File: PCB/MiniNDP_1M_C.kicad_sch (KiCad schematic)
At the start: 12 parts, among them J1 Conn_02x20_Odd_Even, U1 HC238, U2 HC4040, U3 HC573, U4 AS6C2008A_DIP32_SOP32

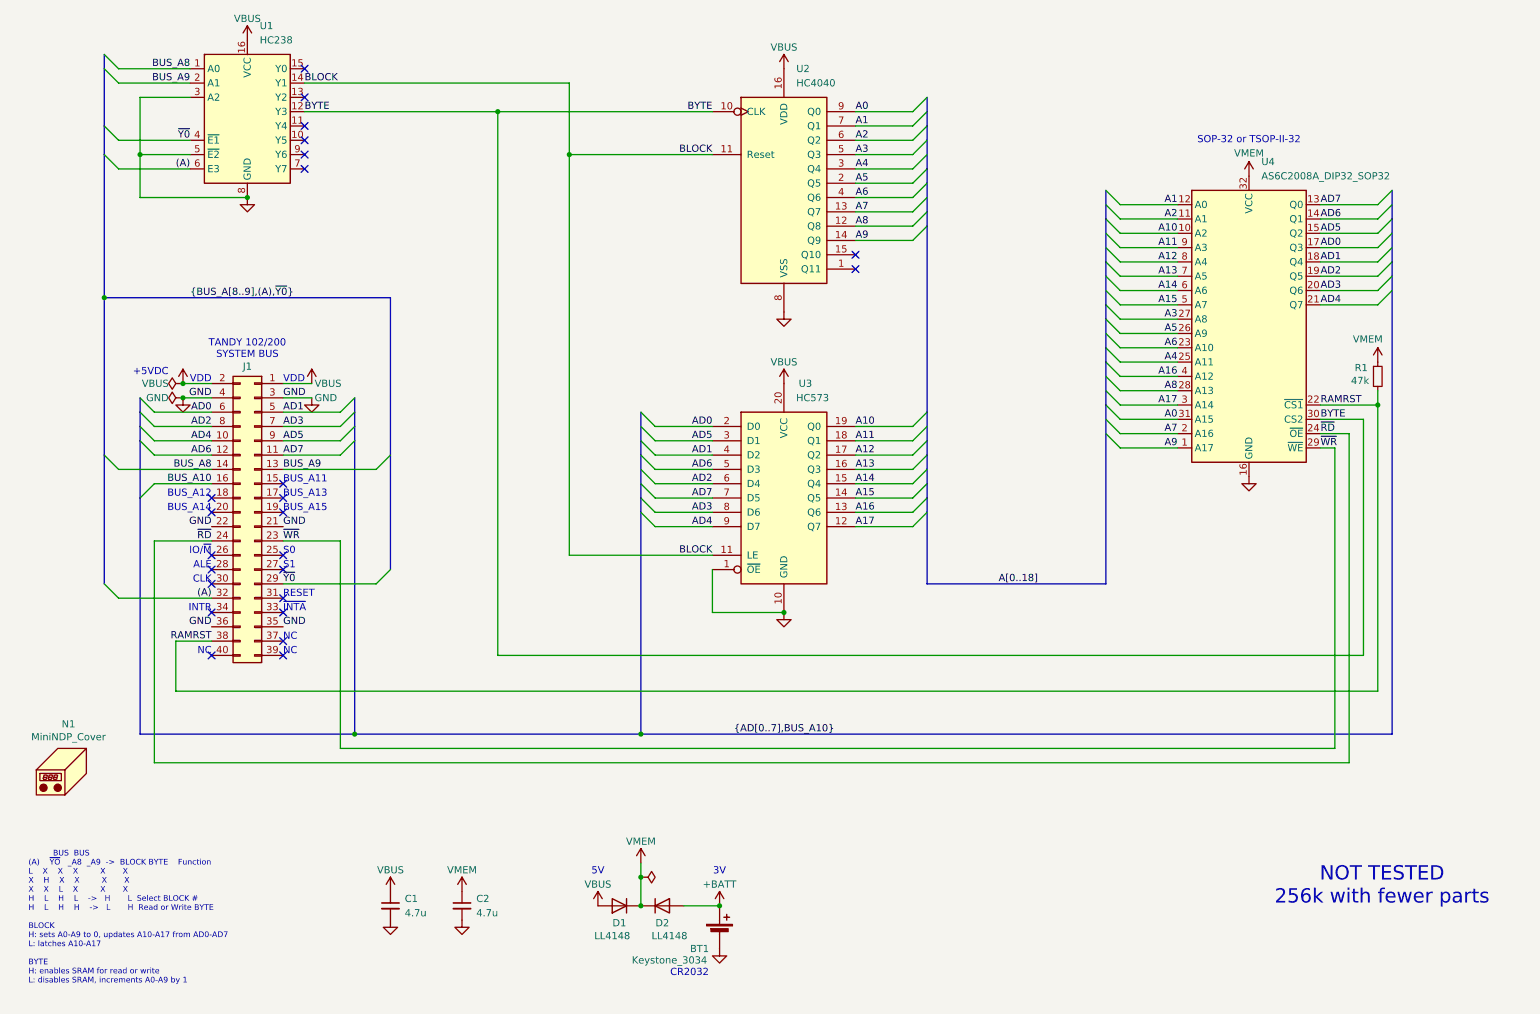
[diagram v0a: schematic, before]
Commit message: 1M_C 1 meg based on 4040
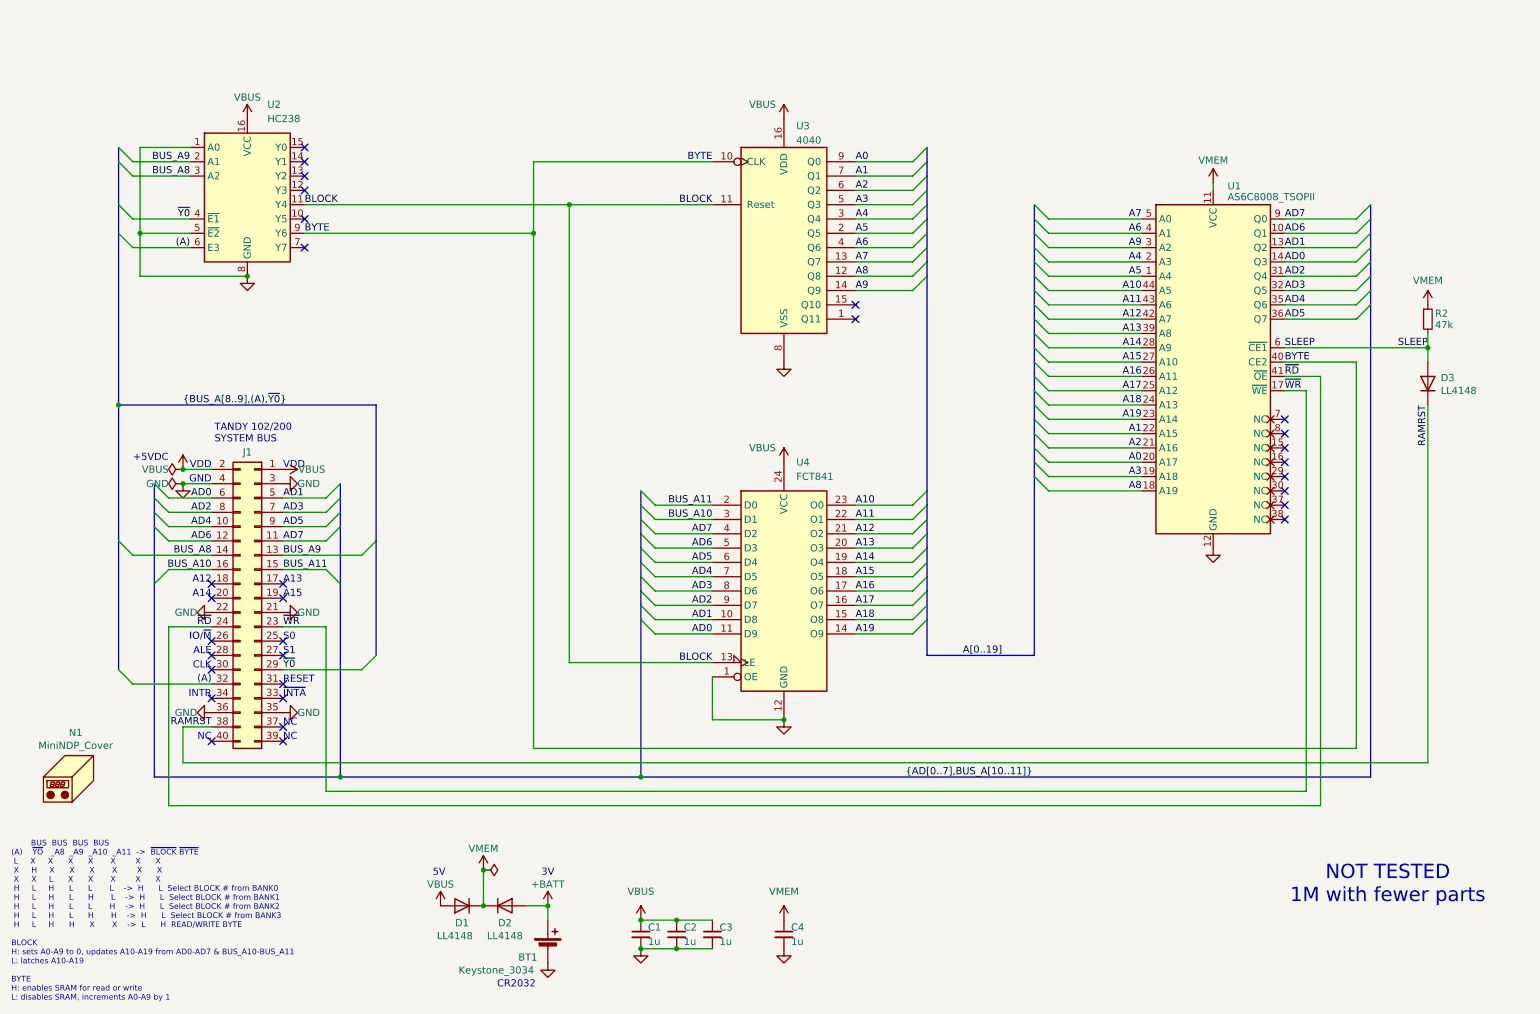
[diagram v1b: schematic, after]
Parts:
- removed R1: 47k, 000_LOCAL:R_1206, symbol 000_LOCAL:R
- removed U1: HC238, 000_LOCAL:SOIC-16_3.9x9.9mm_P1.27mm, symbol 000_LOCAL:74HC238
- removed U2: HC4040, 000_LOCAL:SOIC-16_3.9x9.9mm_P1.27mm, symbol 000_LOCAL:4040
- removed U3: HC573, 000_LOCAL:SOIC-20W_7.5x12.8mm_P1.27mm, symbol 000_LOCAL:74x573
- removed U4: AS6C2008A_DIP32_SOP32, 000_LOCAL:TSOP-II-SOP-32_dual, symbol 000_LOCAL:AS6C2008A_DIP32_SOP32
- added C3, C4: 1u, 000_LOCAL:C_0805, symbol 000_LOCAL:C
- added D3: LL4148, 000_LOCAL:D_MiniMELF, symbol 000_LOCAL:LL4148
- added R2: 47k, 000_LOCAL:R_0805, symbol 000_LOCAL:R
- added U1: AS6C8008_TSOPII, 000_LOCAL:TSOP-II-44, symbol 000_LOCAL:AS6C8008_TSOPII
- added U2: HC238, 000_LOCAL:SOIC-16_3.9x9.9mm_P1.27mm, symbol 000_LOCAL:HC238
- added U3: 4040, 000_LOCAL:SOIC-16_3.9x9.9mm_P1.27mm, symbol 000_LOCAL:4040
- added U4: FCT841, 000_LOCAL:SOIC-24, symbol 000_LOCAL:FCT841
- C1, C2: value 4.7u -> 1u; footprint 000_LOCAL:C_1206 -> 000_LOCAL:C_0805; MPN CL31B475KAHNNNE -> CL21B105KAFNNNE
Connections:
- net (A): now also U2.6 (E3)
- net A0: now also U1.20 (A17), U3.9 (Q0)
- net A1: now also U1.22 (A15), U3.7 (Q1)
- net A10: now also U1.44 (A5), U4.23 (O0)
- net A11: now also U1.43 (A6), U4.22 (O1)
- net A12: now also U1.42 (A7), U4.21 (O2)
- net A13: now also U1.39 (A8), U4.20 (O3)
- net A14: now also U1.28 (A9), U4.19 (O4)
- net A15: now also U1.27 (A10), U4.18 (O5)
- net A16: now also U1.26 (A11), U4.17 (O6)
- net A17: now also U1.25 (A12), U4.16 (O7)
- net A2: now also U1.21 (A16), U3.6 (Q2)
- net A3: now also U1.19 (A18), U3.5 (Q3)
- net A4: now also U1.2 (A3), U3.3 (Q4)
- net A5: now also U1.1 (A4), U3.2 (Q5)
- net A6: now also U1.4 (A1), U3.4 (Q6)
- net A7: now also U1.5 (A0), U3.13 (Q7)
- net A8: now also U1.18 (A19), U3.12 (Q8)
- net A9: now also U1.3 (A2), U3.14 (Q9)
- net AD0: now also U1.14 (Q3), U4.11 (D9)
- net AD1: now also U1.13 (Q2), U4.10 (D8)
- net AD2: now also U1.31 (Q4), U4.9 (D7)
- net AD3: now also U1.32 (Q5), U4.8 (D6)
- net AD4: now also U1.35 (Q6), U4.7 (D5)
- net AD5: now also U1.36 (Q7), U4.6 (D4)
- net AD6: now also U1.10 (Q1), U4.5 (D3)
- net AD7: now also U1.9 (Q0), U4.4 (D2)
- net BLOCK: now also U2.11 (Y4), U3.11 (Reset), U4.13 (LE)
- net BUS_A10: now also U4.3 (D1)
- net BUS_A8: now also U2.3 (A2)
- net BUS_A9: now also U2.2 (A1)
- net BYTE: now also U1.40 (CE2), U2.9 (Y6), U3.10 (CLK)
- net GND: now also C3.2, C4.2, U1.12 (GND), U1.34 (GND), U2.1 (A0), U2.5 (~{E2}), U2.8 (GND), U3.8 (VSS), U4.1 (OE), U4.12 (GND)
- net RAMRST: now also D3.1 (K)
- net VBUS: now also C2.1, C3.1, U2.16 (VCC), U3.16 (VDD), U4.24 (VCC)
- net VMEM: now also C4.1, R2.1, U1.11 (VCC), U1.33 (VCC); no longer C2.1
- net ~{RD}: now also U1.41 (~{OE})
- net ~{WR}: now also U1.17 (~{WE})
- net ~{Y0}: now also U2.4 (~{E1})
- net BUS_A11: now reaches J1.15 (Pin_15)
- net BUS_A11: now also U4.2 (D0)
- new net A18: U1.24 (A13), U4.15 (O8)
- new net A19: U1.23 (A14), U4.14 (O9)
- new net SLEEP: D3.2 (A), R2.2, U1.6 (~{CE1})
- no-connect marks 24 -> 31
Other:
- note added: "A12"
- note added: "A13"
- note added: "A14"
- note added: "A15"
- note added: "BUS BUS BUS BUS (A) ~{YO} _A8 _A9 _A10 _A11 -> ~{BLOCK} ~{BYTE} L X X X X X X X X H X X X X X X X X L X X X X X H L H L L L -> H L Select BLOCK # from BANK0 H L H L H L -> H L Select BLOCK # from BANK1 H L H L L H -> H L Select BLOCK # from BANK2 H L H L H H -> H L Select BLOCK # from BANK3 H L H H X X -> L H READ/WRITE BYTE BLOCK H: sets A0-A9 to 0, updates A10-A19 from AD0-AD7 & BUS_A10-BUS_A11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"
- note added: "GND"
- note added: "NOT TESTED 1M with fewer parts"
- note removed: "BUS BUS (A) ~{YO} _A8 _A9 -> BLOCK BYTE Function L X X X X X X H X X X X X X L X X X H L H L -> H L Select BLOCK # H L H H -> L H Read or Write BYTE BLOCK H: sets A0-A9 to 0, updates A10-A17 from AD0-AD7 L: latches A10-A17 BYTE H: enables SRAM for read or write L: disables SRAM, increments A0-A9 by 1"
- note removed: "BUS_A11"
- note removed: "BUS_A12"
- note removed: "BUS_A13"
- note removed: "BUS_A14"
- note removed: "BUS_A15"
- note removed: "NOT TESTED 256k with fewer parts"
- note removed: "SOP-32 or TSOP-II-32"
- title: MiniNDP 256 -> MiniNDP 1M
- moved on the sheet: J1

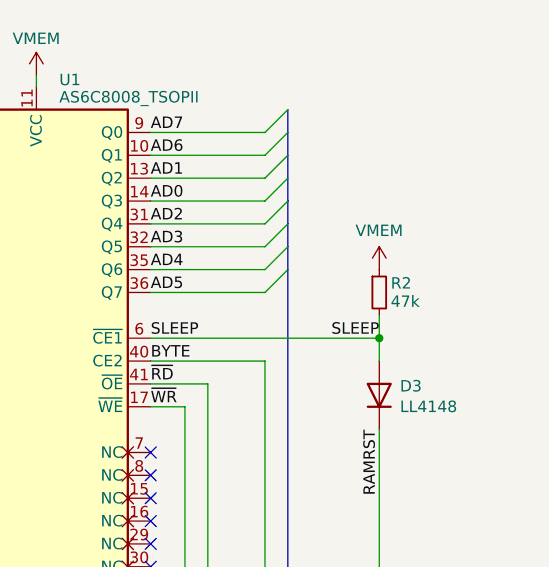
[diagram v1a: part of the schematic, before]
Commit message: 1M_C pwr & gnd traces
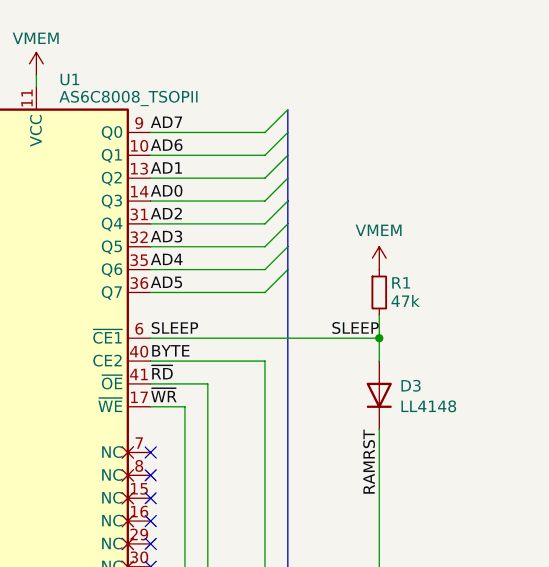
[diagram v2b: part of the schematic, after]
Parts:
- renumbered R2 to R1
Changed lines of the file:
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@@
 		(on_board yes)
 		(dnp no)
-		(property "Reference" "R2"
+		(property "Reference" "R1"
 			(at 267.97 72.644 0)
 			(effects
@@
 			(project "MiniNDP_1M_B"
 				(path "/f15c2929-5cf4-4b4e-965d-148e1bec8a42"
-					(reference "R2")
+					(reference "R1")
 					(unit 1)
 				)
